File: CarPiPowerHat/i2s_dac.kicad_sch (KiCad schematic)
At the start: 23 parts, among them J8 AudioJack2_Ground, Q4 DMG2305, U7 AP2112-3.3K, U8 UDA1334ATS

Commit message: Finished Layout
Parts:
- C28, C31: footprint Capacitor_SMD:C_0805_2012Metric_Pad1.18x1.45mm_HandSolder -> Capacitor_SMD:C_0805_2012Metric
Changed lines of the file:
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@@
     (property "Reference" "C28" (id 0) (at 56.13 161.31 90))
     (property "Value" "10uF" (id 1) (at 60.72 161.31 90))
-    (property "Footprint" "Capacitor_SMD:C_0805_2012Metric_Pad1.18x1.45mm_HandSolder" (id 2) (at 58.42 162.56 0)
+    (property "Footprint" "Capacitor_SMD:C_0805_2012Metric" (id 2) (at 58.42 162.56 0)
       (effects (font (size 1.27 1.27)) hide)
     )
@@
     (property "Reference" "C31" (id 0) (at 91.69 156.23 90))
     (property "Value" "10uF" (id 1) (at 96.28 156.23 90))
-    (property "Footprint" "Capacitor_SMD:C_0805_2012Metric_Pad1.18x1.45mm_HandSolder" (id 2) (at 93.98 157.48 0)
+    (property "Footprint" "Capacitor_SMD:C_0805_2012Metric" (id 2) (at 93.98 157.48 0)
       (effects (font (size 1.27 1.27)) hide)
     )

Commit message: Added part numbers
* Selected parts from lcsc
* Checked footprints
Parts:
- C27, C30, C32: LCSC C14663 -> C14663
- C28, C31: Field4 (none) -> Digikey; Field6 (none) -> GRM21BR71A106KA73L; LCSC (none) -> C15850
- C29, C35: Field4 (none) -> Digikey; Field6 (none) -> GRM21BR71A106KA73L
- C34: LCSC C134775 -> C164078
- Q4: value DMG2305 -> DMG2305; footprint Package_TO_SOT_SMD:SOT-23W_Handsoldering -> Package_TO_SOT_SMD:SOT-23
- R22: LCSC (none) -> C25804; LSCSC C25804 -> (none)
- R23: footprint Resistor_SMD:R_0603_1608Metric_Pad0.98x0.95mm_HandSolder -> Resistor_SMD:R_0603_1608Metric
- R26, R27: LCSC C22775 -> C22775
- U7: LCSC (none) -> C51118
- U8: LCSC (none) -> C494494
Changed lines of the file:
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@@
       (effects (font (size 1.27 1.27)) hide)
     )
-    (property "LSCSC" "C25804" (id 4) (at 56.515 78.74 0)
+    (property "LCSC" "C25804" (id 4) (at 56.515 78.74 0)
       (effects (font (size 1.27 1.27)) hide)
     )
@@
       (effects (font (size 1.016 1.016) bold))
     )
-    (property "Footprint" "Resistor_SMD:R_0603_1608Metric_Pad0.98x0.95mm_HandSolder" (id 2) (at 65.913 109.22 90)
+    (property "Footprint" "Resistor_SMD:R_0603_1608Metric" (id 2) (at 65.913 109.22 90)
       (effects (font (size 1.27 1.27)) hide)
     )
@@
       (effects (font (size 1.27 1.27)) hide)
     )
-    (property "LCSC" " C22775" (id 4) (at 142.875 63.5 0)
+    (property "LCSC" "C22775" (id 4) (at 142.875 63.5 0)
       (effects (font (size 1.27 1.27)) hide)
     )
@@
       (effects (font (size 1.27 1.27)) hide)
     )
-    (property "LCSC" " C22775" (id 4) (at 142.875 83.82 0)
+    (property "LCSC" "C22775" (id 4) (at 142.875 83.82 0)
       (effects (font (size 1.27 1.27)) hide)
     )
@@
       (effects (font (size 1.27 1.27)) hide)
     )
+    (property "Field4" "Digikey" (id 4) (at 58.42 162.56 0)
+      (effects (font (size 1.27 1.27)) hide)
+    )
+    (property "Field6" "GRM21BR71A106KA73L" (id 5) (at 58.42 162.56 0)
+      (effects (font (size 1.27 1.27)) hide)
+    )
+    (property "LCSC" "C15850" (id 6) (at 58.42 162.56 0)
+      (effects (font (size 1.27 1.27)) hide)
+    )
     (pin "1")
     (pin "2")
@@
       (effects (font (size 1.27 1.27)) hide)
     )
+    (property "Field4" "Digikey" (id 4) (at 93.98 157.48 0)
+      (effects (font (size 1.27 1.27)) hide)
+    )
+    (property "Field6" "GRM21BR71A106KA73L" (id 5) (at 93.98 157.48 0)
+      (effects (font (size 1.27 1.27)) hide)
+    )
+    (property "LCSC" "C15850" (id 6) (at 93.98 157.48 0)
+      (effects (font (size 1.27 1.27)) hide)
+    )
     (pin "1")
     (pin "2")
@@
       (effects (font (size 1.27 1.27)) hide)
     )
+    (property "Field4" "Digikey" (id 5) (at 132.715 111.76 0)
+      (effects (font (size 1.27 1.27)) hide)
+    )
+    (property "Field6" "GRM21BR71A106KA73L" (id 6) (at 132.715 111.76 0)
+      (effects (font (size 1.27 1.27)) hide)
+    )
     (pin "1")
     (pin "2")
@@
       (effects (font (size 1.27 1.27)) hide)
     )
-    (property "LCSC" " C14663" (id 4) (at 57.785 58.42 90)
+    (property "LCSC" "C14663" (id 4) (at 57.785 58.42 90)
       (effects (font (size 1.27 1.27)) hide)
     )
@@
       (effects (font (size 1.27 1.27)) hide)
     )
+    (property "Field4" "Digikey" (id 5) (at 78.105 50.8 0)
+      (effects (font (size 1.27 1.27)) hide)
+    )
+    (property "Field6" "GRM21BR71A106KA73L" (id 6) (at 78.105 50.8 0)
+      (effects (font (size 1.27 1.27)) hide)
+    )
     (pin "1")
     (pin "2")
@@
       (effects (font (size 1.27 1.27)) hide)
     )
-    (property "LCSC" " C14663" (id 4) (at 78.105 58.42 90)
+    (property "LCSC" "C14663" (id 4) (at 78.105 58.42 90)
       (effects (font (size 1.27 1.27)) hide)
     )
@@
       (effects (font (size 1.27 1.27)) hide)
     )
-    (property "LCSC" " C14663" (id 4) (at 125.095 110.49 90)
+    (property "LCSC" "C14663" (id 4) (at 125.095 110.49 90)
       (effects (font (size 1.27 1.27)) hide)
     )
@@
       (effects (font (size 1.27 1.27)) hide)
     )
-    (property "LCSC" "C134775" (id 4) (at 128.905 83.82 90)
+    (property "LCSC" "C164078" (id 4) (at 128.905 83.82 90)
       (effects (font (size 1.27 1.27)) hide)
     )
@@
       (effects (font (size 1.27 1.0795)) (justify left bottom))
     )
-    (property "Value" " DMG2305" (id 1) (at 66.929 90.805 0)
+    (property "Value" "DMG2305" (id 1) (at 66.929 90.805 0)
       (effects (font (size 1.27 1.0795)) (justify left bottom))
     )
-    (property "Footprint" "Package_TO_SOT_SMD:SOT-23W_Handsoldering" (id 2) (at 64.135 88.9 0)
+    (property "Footprint" "Package_TO_SOT_SMD:SOT-23" (id 2) (at 64.135 88.9 0)
       (effects (font (size 1.27 1.27)) hide)
     )
@@
       (effects (font (size 1.27 1.27)) hide)
     )
+    (property "LCSC" "C51118" (id 4) (at 76.2 154.94 0)
+      (effects (font (size 1.27 1.27)) hide)
+    )
     (pin "1")
     (pin "2")
@@
       (effects (font (size 1.27 1.27)) hide)
     )
+    (property "LCSC" "C494494" (id 4) (at 107.315 83.82 0)
+      (effects (font (size 1.27 1.27)) hide)
+    )

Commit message: Fixed some bugs, not done yet
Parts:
- renumbered C31 to C20, C30 to C21, C33 to C22, C28 to C23, C29 to C24, C32 to C25, C35 to C28, C36 to C35, C37 to C36, FB4 to FB2, J8 to J4, Q4 to Q3, R24 to R15, R22 to R16, R23 to R18, R26 to R25, R25 to R26, U7 to U5, U8 to U6
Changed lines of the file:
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@@
   (symbol (lib_id "Adafruit I2S Audio UDA1334 Bonnet-eagle-import:FERRITE0805") (at 84.455 43.18 90) (unit 1)
     (in_bom yes) (on_board yes)
-    (property "Reference" "FB4" (id 0) (at 82.55 44.45 0)
+    (property "Reference" "FB2" (id 0) (at 82.55 44.45 0)
       (effects (font (size 1.27 1.0795)) (justify left bottom))
     )
@@
   (symbol (lib_id "Device:R") (at 56.515 78.74 90) (unit 1)
     (in_bom yes) (on_board yes)
-    (property "Reference" "R22" (id 0) (at 53.975 78.74 0))
+    (property "Reference" "R16" (id 0) (at 53.975 78.74 0))
     (property "Value" "10K" (id 1) (at 56.515 78.74 0)
       (effects (font (size 1.016 1.016) bold))
@@
   (symbol (lib_id "Device:R") (at 64.135 109.22 180) (unit 1)
     (in_bom yes) (on_board yes)
-    (property "Reference" "R23" (id 0) (at 64.135 111.76 0))
+    (property "Reference" "R18" (id 0) (at 64.135 111.76 0))
     (property "Value" "10K" (id 1) (at 64.135 109.22 0)
       (effects (font (size 1.016 1.016) bold))
@@
   (symbol (lib_id "Device:R") (at 135.255 71.12 180) (unit 1)
     (in_bom yes) (on_board yes)
-    (property "Reference" "R24" (id 0) (at 135.255 73.66 0))
+    (property "Reference" "R15" (id 0) (at 135.255 73.66 0))
     (property "Value" "220k" (id 1) (at 135.255 71.12 0)
       (effects (font (size 1.016 1.016) bold))
@@
   (symbol (lib_id "Device:R") (at 135.255 91.44 180) (unit 1)
     (in_bom yes) (on_board yes)
-    (property "Reference" "R25" (id 0) (at 135.255 93.98 0))
+    (property "Reference" "R26" (id 0) (at 135.255 93.98 0))
     (property "Value" "220k" (id 1) (at 135.255 91.44 0)
       (effects (font (size 1.016 1.016) bold))
@@
   (symbol (lib_id "Device:R") (at 142.875 63.5 90) (unit 1)
     (in_bom yes) (on_board yes)
-    (property "Reference" "R26" (id 0) (at 140.335 63.5 0))
+    (property "Reference" "R25" (id 0) (at 140.335 63.5 0))
     (property "Value" "100" (id 1) (at 142.875 63.5 0)
       (effects (font (size 1.016 1.016) bold))
@@
   (symbol (lib_id "Adafruit I2S Audio UDA1334 Bonnet-eagle-import:CAP_CERAMIC0805-NOOUTLINE") (at 58.42 162.56 0) (unit 1)
     (in_bom yes) (on_board yes)
-    (property "Reference" "C28" (id 0) (at 56.13 161.31 90))
+    (property "Reference" "C23" (id 0) (at 56.13 161.31 90))
     (property "Value" "10uF" (id 1) (at 60.72 161.31 90))
     (property "Footprint" "Capacitor_SMD:C_0805_2012Metric" (id 2) (at 58.42 162.56 0)
@@
   (symbol (lib_id "Adafruit I2S Audio UDA1334 Bonnet-eagle-import:CAP_CERAMIC0805-NOOUTLINE") (at 93.98 157.48 0) (unit 1)
     (in_bom yes) (on_board yes)
-    (property "Reference" "C31" (id 0) (at 91.69 156.23 90))
+    (property "Reference" "C20" (id 0) (at 91.69 156.23 90))
     (property "Value" "10uF" (id 1) (at 96.28 156.23 90))
     (property "Footprint" "Capacitor_SMD:C_0805_2012Metric" (id 2) (at 93.98 157.48 0)
@@
   (symbol (lib_id "Adafruit I2S Audio UDA1334 Bonnet-eagle-import:CAP_CERAMIC0805-NOOUTLINE") (at 132.715 111.76 0) (unit 1)
     (in_bom yes) (on_board yes)
-    (property "Reference" "C35" (id 0) (at 130.425 110.51 90))
+    (property "Reference" "C28" (id 0) (at 130.425 110.51 90))
     (property "Value" "10uF" (id 1) (at 135.015 110.51 90))
     (property "Footprint" "Capacitor_SMD:C_0805_2012Metric" (id 2) (at 132.715 111.76 0)
@@
   (symbol (lib_id "Device:C") (at 78.105 50.8 270) (unit 1)
     (in_bom yes) (on_board yes)
-    (property "Reference" "C29" (id 0) (at 79.355 48.51 90))
+    (property "Reference" "C24" (id 0) (at 79.355 48.51 90))
     (property "Value" "10uF" (id 1) (at 79.355 53.1 90))
     (property "Footprint" "Capacitor_SMD:C_0805_2012Metric" (id 2) (at 74.295 51.7652 0)
@@
   (symbol (lib_id "Device:C") (at 78.105 58.42 270) (unit 1)
     (in_bom yes) (on_board yes)
-    (property "Reference" "C30" (id 0) (at 79.355 56.13 90))
+    (property "Reference" "C21" (id 0) (at 79.355 56.13 90))
     (property "Value" "0.1uF" (id 1) (at 79.355 60.72 90))
     (property "Footprint" "Capacitor_SMD:C_0603_1608Metric" (id 2) (at 74.295 59.3852 0)
@@
   (symbol (lib_id "Device:C") (at 125.095 110.49 0) (unit 1)
     (in_bom yes) (on_board yes)
-    (property "Reference" "C32" (id 0) (at 122.805 109.24 90))
+    (property "Reference" "C25" (id 0) (at 122.805 109.24 90))
     (property "Value" "0.1uF" (id 1) (at 127.395 109.24 90))
     (property "Footprint" "Capacitor_SMD:C_0603_1608Metric" (id 2) (at 126.0602 114.3 0)
@@
   (symbol (lib_id "Device:C_Polarized") (at 128.905 63.5 90) (mirror x) (unit 1)
     (in_bom yes) (on_board yes)
-    (property "Reference" "C33" (id 0) (at 127.655 61.11 90))
+    (property "Reference" "C22" (id 0) (at 127.655 61.11 90))
     (property "Value" "47uF" (id 1) (at 127.655 66 90))
     (property "Footprint" "Capacitor_SMD:CP_Elec_6.3x7.7" (id 2) (at 132.715 64.4652 0)
@@
   (symbol (lib_id "Device:C") (at 150.495 69.85 0) (unit 1)
     (in_bom yes) (on_board yes)
-    (property "Reference" "C36" (id 0) (at 148.205 68.6 90))
+    (property "Reference" "C35" (id 0) (at 148.205 68.6 90))
     (property "Value" "0.01uF" (id 1) (at 152.795 68.6 90))
     (property "Footprint" "Capacitor_SMD:C_0603_1608Metric" (id 2) (at 151.4602 73.66 0)
@@
   (symbol (lib_id "Device:C") (at 150.495 90.17 0) (unit 1)
     (in_bom yes) (on_board yes)
-    (property "Reference" "C37" (id 0) (at 148.205 88.92 90))
+    (property "Reference" "C36" (id 0) (at 148.205 88.92 90))
     (property "Value" "0.01uF" (id 1) (at 152.795 88.92 90))
     (property "Footprint" "Capacitor_SMD:C_0603_1608Metric" (id 2) (at 151.4602 93.98 0)
@@
   (symbol (lib_id "Adafruit I2S Audio UDA1334 Bonnet-eagle-import:MOSFET-PWIDE") (at 64.135 88.9 0) (unit 1)
     (in_bom yes) (on_board yes)
-    (property "Reference" "Q4" (id 0) (at 66.929 88.519 0)
+    (property "Reference" "Q3" (id 0) (at 66.929 88.519 0)
       (effects (font (size 1.27 1.0795)) (justify left bottom))
     )
@@
   (symbol (lib_id "Connector:AudioJack3_Ground") (at 202.565 68.58 180) (unit 1)
     (in_bom yes) (on_board yes)
-    (property "Reference" "J8" (id 0) (at 201.803 76.835 0))
+    (property "Reference" "J4" (id 0) (at 201.803 76.835 0))
     (property "Value" "AudioJack2_Ground" (id 1) (at 201.803 74.295 0))
     (property "Footprint" "Connector_Audio:Jack_3.5mm_CUI_SJ-3524-SMT_Horizontal" (id 2) (at 202.565 68.58 0)
@@
   (symbol (lib_id "Adafruit I2S Audio UDA1334 Bonnet-eagle-import:VREG_SOT23-5") (at 76.2 154.94 0) (unit 1)
     (in_bom yes) (on_board yes)
-    (property "Reference" "U7" (id 0) (at 68.58 148.844 0)
+    (property "Reference" "U5" (id 0) (at 68.58 148.844 0)
       (effects (font (size 1.27 1.0795)) (justify left bottom))
     )
@@
   (symbol (lib_id "Adafruit I2S Audio UDA1334 Bonnet-eagle-import:AUDIO_I2S_UDA1334__") (at 107.315 83.82 0) (unit 1)
     (in_bom yes) (on_board yes)
-    (property "Reference" "U8" (id 0) (at 94.615 54.61 0)
-      (effects (font (size 1.778 1.5113)) (justify left bottom))
-    )
+    (property "Reference" "U6" (id 0) (at 94.615 54.61 0)
+      (effects (font (size 1.778 1.5113)) (justify left bottom))
+    )

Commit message: Finalized 2.2
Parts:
- removed C20, C23: 10uF, Capacitor_SMD:C_0805_2012Metric, symbol Adafruit I2S Audio UDA1334 Bonnet-eagle-import:CAP_CERAMIC0805-NOOUTLINE
- removed U5: AP2112-3.3K, Package_TO_SOT_SMD:SOT-23-5_HandSoldering, symbol Adafruit I2S Audio UDA1334 Bonnet-eagle-import:VREG_SOT23-5
- added C20, C23: 1uF, Capacitor_SMD:C_0805_2012Metric_Pad1.18x1.45mm_HandSolder, symbol Device:C
- added U5: XC6206P332MR, Package_TO_SOT_SMD:SOT-23, symbol Regulator_Linear:XC6206PxxxMR
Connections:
- net +5v: now also C20.1, U5.3 (VI)
- net GND: now also C20.2, C23.2, U5.1 (GND)
- net VDDA: now also C23.1, U5.2 (VO)
- no-connect marks 1 -> 0

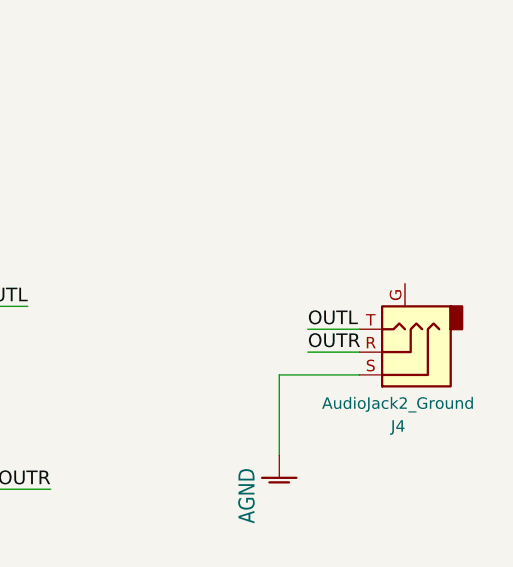
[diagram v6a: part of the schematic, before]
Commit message: Finalizing, checking parts
Might be ready for production
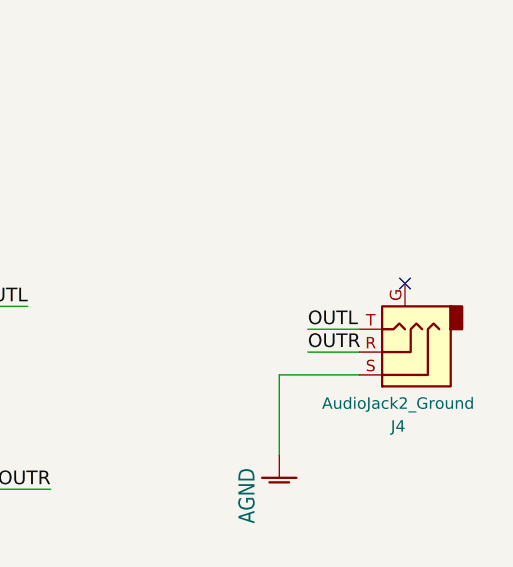
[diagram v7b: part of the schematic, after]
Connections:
- no-connect marks 0 -> 1
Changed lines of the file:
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@@
   (junction (at 150.495 83.82) (diameter 0.9144) (color 0 0 0 0))
   (junction (at 167.005 127.635) (diameter 0.9144) (color 0 0 0 0))
+  (no_connect (at 202.565 60.96))
   (wire (pts (xy 46.355 58.42) (xy 46.355 60.96))
     (stroke (width 0) (type solid) (color 0 0 0 0))
